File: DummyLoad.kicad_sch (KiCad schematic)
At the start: 31 parts, among them J1 RF In, J2 RF Out, J3 Conn_01x02_Pin

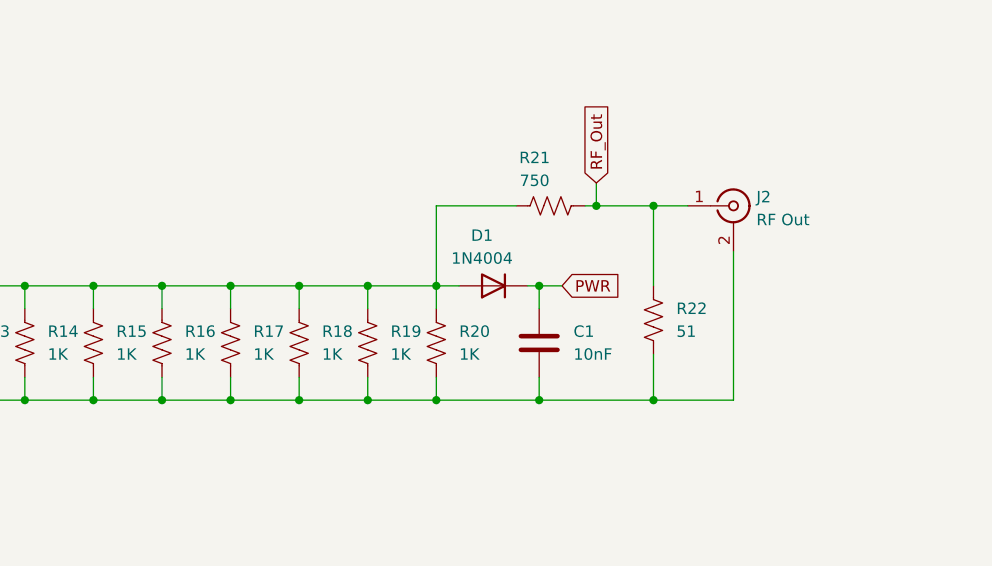
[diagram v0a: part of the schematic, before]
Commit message: Schematic: add symbols, ground & rewire
Modify DummyLoad.kicad_sch: add new symbols and power net, reposition several components and update wiring/junctions. Added Device:R_US instances (R24, R23), a power:GND symbol that creates a global GND label, and multiple junction/wire elements to re-route nets (including RF_Out and PWR). Removed a few redundant junctions/wires and updated component coordinates/UUIDs to reflect the new layout. These changes reorganize the sheet wiring and place new parts for the updated schematic topology.
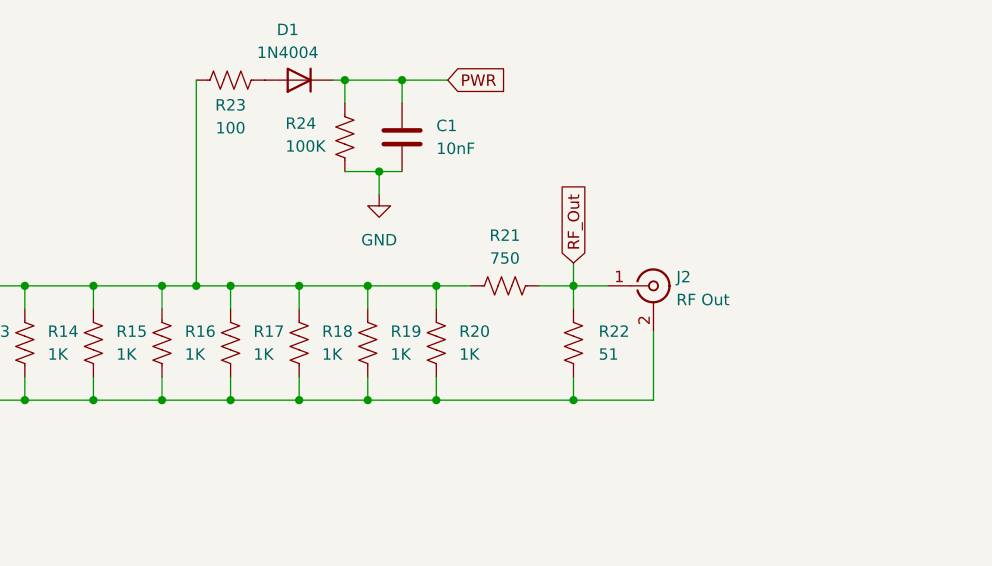
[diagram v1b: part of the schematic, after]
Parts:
- added R23: 100, symbol Device:R_US
- added R24: 100K, symbol Device:R_US
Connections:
- net GND: now also R24.2
- net PWR: now also R24.1
- net RF_In: now also R23.2; no longer D1.2 (A)
- new net: D1.2 (A), R23.1
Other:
- moved on the sheet: C1, D1, J2, R21, R22

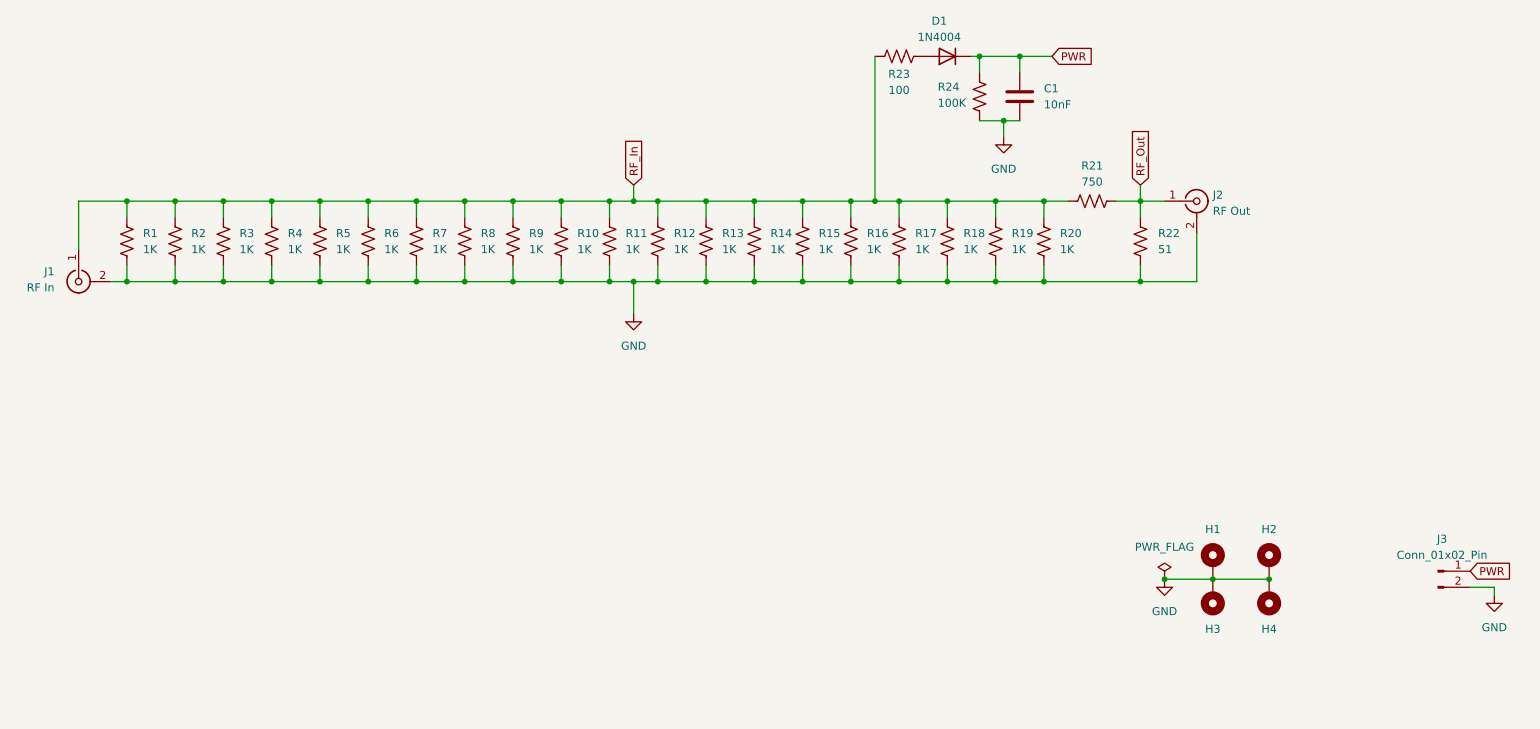
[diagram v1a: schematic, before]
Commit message: Schematic: update layout & title block
Set paper to USLetter and add a title block (title, date, revision, company and descriptive comments). Perform a large schematic redraw: many junctions, wires and their coordinates were moved and multiple UUIDs updated/renamed. Changes appear to be layout/coordinate and metadata updates rather than functional/electrical modifications.
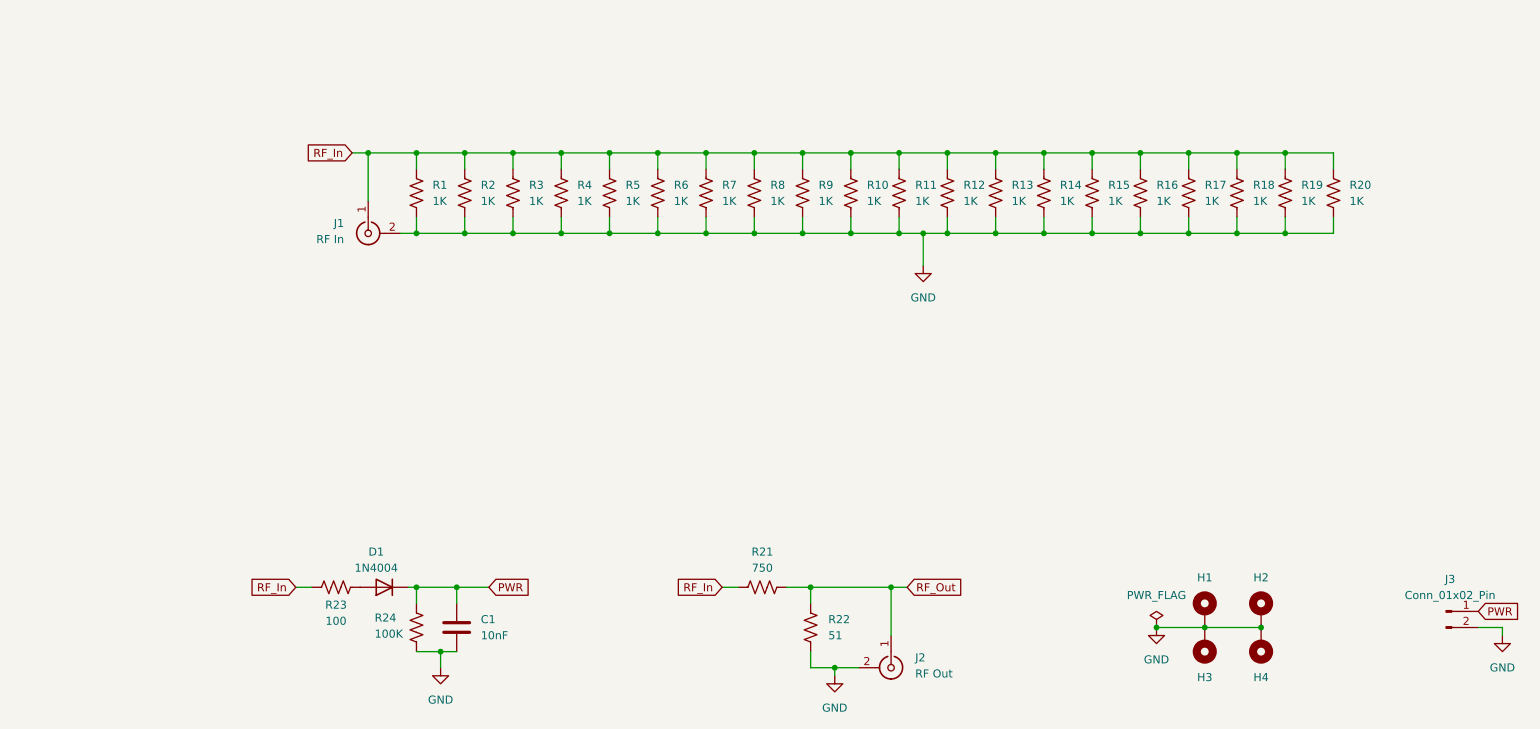
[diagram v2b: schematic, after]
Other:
- company: (none) -> NE3U
- title: (none) -> Dummy Load
- moved on the sheet: C1, D1, H1, H2, H3, H4, J1, J2, J3, R1, R10, R11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

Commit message: Refactor connector, testpoints and layout
Replace generic connector symbols with coaxial/TestPoint symbols and tidy schematic metadata; adjust component positions, wires and junctions, and update footprints/datasheets/Mouser PNs. Added text annotations (Mounting Holes, 50 Ohm Dummy Load, attenuation/measurement notes), new testpoint symbols/instances and a few resistor symbols/instances, renamed/updated some references (e.g. R24 -> R26) and moved mounting holes and global label locations to match the revised layout. These changes improve part accuracy, footprints and documentation in the DummyLoad.kicad_sch.
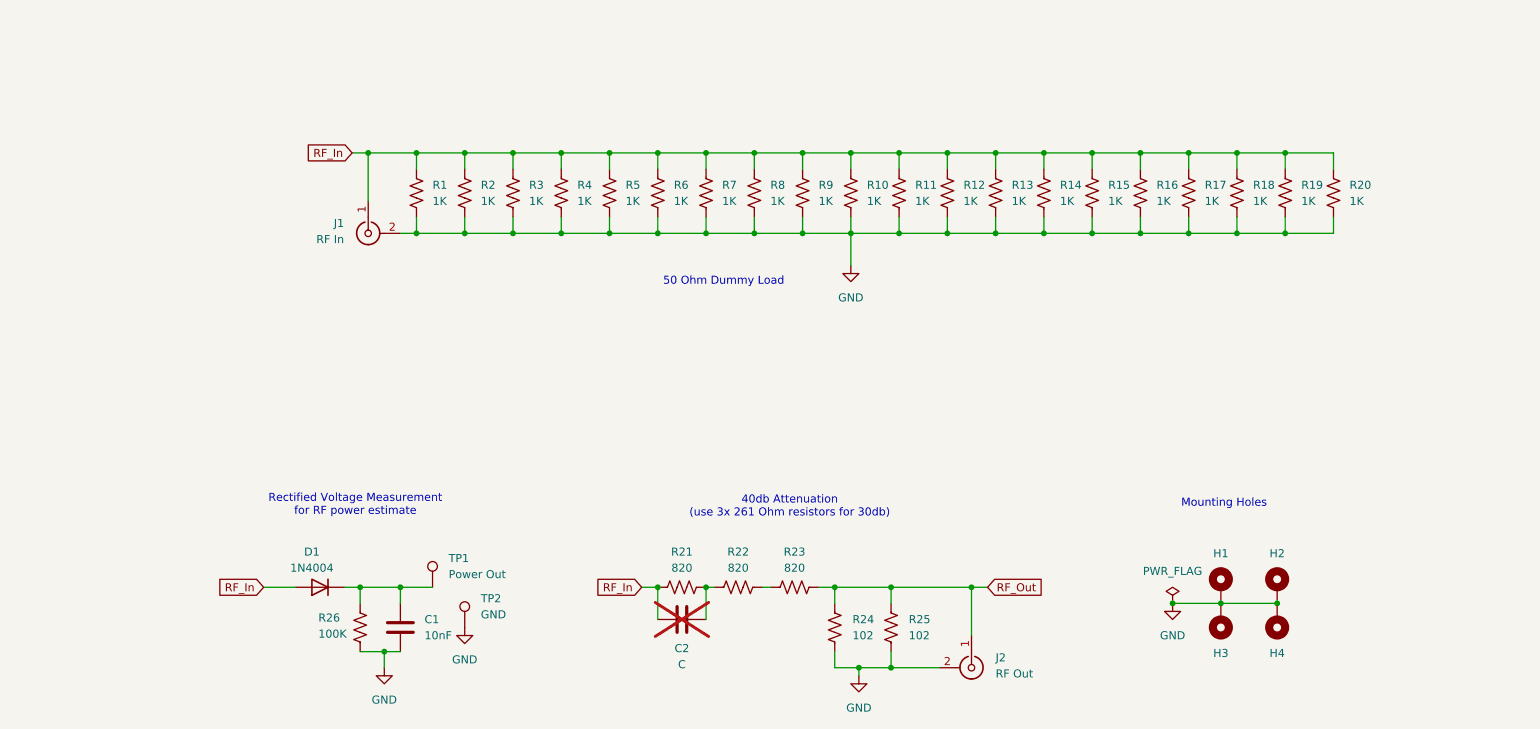
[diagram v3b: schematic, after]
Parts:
- removed J3: Conn_01x02_Pin, Connector_PinHeader_2.54mm:PinHeader_1x02_P2.54mm_Vertical, symbol Connector:Conn_01x02_Pin
- removed R23: 100, symbol Device:R_US
- added C2: C, Capacitor_SMD:C_1206_3216Metric, symbol Device:C
- added R21, R22: 820, Resistor_SMD:R_1206_3216Metric, symbol Device:R_US
- added R25: 102, Resistor_SMD:R_1206_3216Metric, symbol Device:R_US
- added TP1: Power Out, symbol Connector:TestPoint
- added TP2: GND, symbol Connector:TestPoint
- C1: Mouser PN (none) -> 77-VJ1206Y103JXAMP
- D1: Mouser PN (none) -> 583-FM4004
- J1, J2: Mouser PN (none) -> 737-RF101KD0050BKHDW
- R23: renamed from R21; value 750 -> 820; Mouser PN 708-RNCP1206FTD750R -> 279-CRGH1206F820R
- R24: renamed from R22; value 51 -> 102; Mouser PN (none) -> 667-ERJ-8ENF1020V
- R26: renamed from R24; footprint (none) -> Resistor_SMD:R_1206_3216Metric; Mouser PN (none) -> 652-CRM1206QFX-1003E
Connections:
- net GND: now also R25.2, TP2.1
- net RF_In: now also D1.2 (A), C2.2, R21.2; no longer R23.2
- net RF_Out: now also R25.1
- net PWR: no longer names the net of C1.1, D1.1 (K), R26.1
- net PWR: now also TP1.1
- new net: R22.1, R23.2
- new net: C2.1, R21.1, R22.2
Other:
- note added: "40db Attenuation (use 3x 261 Ohm resistors for 30db)"
- note added: "50 Ohm Dummy Load"
- note added: "Mounting Holes"
- note added: "Rectified Voltage Measurement for RF power estimate"
- company: NE3U -> Design by NE3U
- moved on the sheet: C1, D1, H1, H2, H3, H4, J2, R23, R24, R26

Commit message: Add THT test point footprints to schematic
Assign the TestPoint footprint to two components in DummyLoad.kicad_sch. Previously the Footprint property was empty; this commit sets it to "TestPoint:TestPoint_THTPad_D1.0mm_Drill0.5mm" for the two entries so exported netlists/PCBs include the intended through-hole test pads.
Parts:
- TP1, TP2: footprint (none) -> TestPoint:TestPoint_THTPad_D1.0mm_Drill0.5mm
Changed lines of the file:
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@@
 			)
 		)
-		(property "Footprint" ""
+		(property "Footprint" "TestPoint:TestPoint_THTPad_D1.0mm_Drill0.5mm"
 			(at 91.44 127 0)
 			(effects
@@
 			)
 		)
-		(property "Footprint" ""
+		(property "Footprint" "TestPoint:TestPoint_THTPad_D1.0mm_Drill0.5mm"
 			(at 86.36 120.65 0)
 			(effects

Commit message: Update component datasheets, PNs, footprints
Update metadata in DummyLoad.kicad_sch: replace generic Vishay datasheet links with the direct rcse3.pdf URL and change Mouser PN from 279-CRGP2512F1K0 to 71-RCS12061K00FKEA across multiple components. Also update one diode entry: change footprint to Diode_SMD:Nexperia_CFP3_SOD-123W, datasheet to 1N5711W.pdf, and Mouser PN to 621-1N5711W-F. These changes correct BOM/reference links and footprints for accurate sourcing.
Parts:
- D1: footprint Diode_SMD:D_SMA -> Diode_SMD:Nexperia_CFP3_SOD-123W; Mouser PN 583-FM4004 -> 621-1N5711W-F
- R1, R10, R11, R12, R13, R14, R15, R16, R17, R18, R19, R2, R20, R3, R4, R5, R6, R7, R8, R9: Mouser PN 279-CRGP2512F1K0 -> 71-RCS12061K00FKEA
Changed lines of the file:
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@@
 			)
 		)
-		(property "Datasheet" "https://www.vishay.com/doc?20065"
+		(property "Datasheet" "https://www.vishay.com/docs/20065/rcse3.pdf"
 			(at 147.32 58.42 0)
 			(effects
@@
 			)
 		)
-		(property "Mouser PN" "279-CRGP2512F1K0"
+		(property "Mouser PN" "71-RCS12061K00FKEA"
 			(at 147.32 58.42 0)
 			(effects
@@
 			)
 		)
-		(property "Datasheet" "https://www.vishay.com/doc?20065"
+		(property "Datasheet" "https://www.vishay.com/docs/20065/rcse3.pdf"
 			(at 162.56 58.42 0)
 			(effects
@@
 			)
 		)
-		(property "Mouser PN" "279-CRGP2512F1K0"
+		(property "Mouser PN" "71-RCS12061K00FKEA"
 			(at 162.56 58.42 0)
 			(effects
@@
 			)
 		)
-		(property "Datasheet" "https://www.vishay.com/doc?20065"
+		(property "Datasheet" "https://www.vishay.com/docs/20065/rcse3.pdf"
 			(at 139.7 58.42 0)
 			(effects
@@
 			)
 		)
-		(property "Mouser PN" "279-CRGP2512F1K0"
+		(property "Mouser PN" "71-RCS12061K00FKEA"
 			(at 139.7 58.42 0)
 			(effects
@@
 			)
 		)
-		(property "Datasheet" "https://www.vishay.com/doc?20065"
+		(property "Datasheet" "https://www.vishay.com/docs/20065/rcse3.pdf"
 			(at 78.74 58.42 0)
 			(effects
@@
 			)
 		)
-		(property "Mouser PN" "279-CRGP2512F1K0"
+		(property "Mouser PN" "71-RCS12061K00FKEA"
 			(at 78.74 58.42 0)
 			(effects
@@
 			)
 		)
-		(property "Datasheet" "https://www.vishay.com/doc?20065"
+		(property "Datasheet" "https://www.vishay.com/docs/20065/rcse3.pdf"
 			(at 86.36 58.42 0)
 			(effects
@@
 			)
 		)
-		(property "Mouser PN" "279-CRGP2512F1K0"
+		(property "Mouser PN" "71-RCS12061K00FKEA"
 			(at 86.36 58.42 0)
 			(effects
@@
 			)
 		)
-		(property "Datasheet" "https://www.vishay.com/doc?20065"
+		(property "Datasheet" "https://www.vishay.com/docs/20065/rcse3.pdf"
 			(at 109.22 58.42 0)
 			(effects
@@
 			)
 		)
-		(property "Mouser PN" "279-CRGP2512F1K0"
+		(property "Mouser PN" "71-RCS12061K00FKEA"
 			(at 109.22 58.42 0)
 			(effects
@@
 			)
 		)
-		(property "Datasheet" "https://www.vishay.com/doc?20065"
+		(property "Datasheet" "https://www.vishay.com/docs/20065/rcse3.pdf"
 			(at 215.9 58.42 0)
 			(effects
@@
 			)
 		)
-		(property "Mouser PN" "279-CRGP2512F1K0"
+		(property "Mouser PN" "71-RCS12061K00FKEA"
 			(at 215.9 58.42 0)
 			(effects
@@
 			)
 		)
-		(property "Datasheet" "https://www.vishay.com/doc?20065"
+		(property "Datasheet" "https://www.vishay.com/docs/20065/rcse3.pdf"
 			(at 177.8 58.42 0)
 			(effects
@@
 			)
 		)
-		(property "Mouser PN" "279-CRGP2512F1K0"
+		(property "Mouser PN" "71-RCS12061K00FKEA"
 			(at 177.8 58.42 0)
 			(effects
@@
 			)
 		)
-		(property "Datasheet" "https://www.vishay.com/doc?20065"
+		(property "Datasheet" "https://www.vishay.com/docs/20065/rcse3.pdf"
 			(at 93.98 58.42 0)
 			(effects
@@
 			)
 		)
-		(property "Mouser PN" "279-CRGP2512F1K0"
+		(property "Mouser PN" "71-RCS12061K00FKEA"
 			(at 93.98 58.42 0)
 			(effects
@@
 			)
 		)
-		(property "Datasheet" "https://www.vishay.com/doc?20065"
+		(property "Datasheet" "https://www.vishay.com/docs/20065/rcse3.pdf"
 			(at 170.18 58.42 0)
 			(effects
@@
 			)
 		)
-		(property "Mouser PN" "279-CRGP2512F1K0"
+		(property "Mouser PN" "71-RCS12061K00FKEA"
 			(at 170.18 58.42 0)
 			(effects
@@
 			)
 		)
-		(property "Datasheet" "https://www.vishay.com/doc?20065"
+		(property "Datasheet" "https://www.vishay.com/docs/20065/rcse3.pdf"
 			(at 116.84 58.42 0)
 			(effects
@@
 			)
 		)
-		(property "Mouser PN" "279-CRGP2512F1K0"
+		(property "Mouser PN" "71-RCS12061K00FKEA"
 			(at 116.84 58.42 0)
 			(effects
@@
 			)
 		)
-		(property "Datasheet" "https://www.vishay.com/doc?20065"
+		(property "Datasheet" "https://www.vishay.com/docs/20065/rcse3.pdf"
 			(at 208.28 58.42 0)
 			(effects
@@
 			)
 		)
-		(property "Mouser PN" "279-CRGP2512F1K0"
+		(property "Mouser PN" "71-RCS12061K00FKEA"
 			(at 208.28 58.42 0)
 			(effects
@@
 			)
 		)
-		(property "Datasheet" "https://www.vishay.com/doc?20065"
+		(property "Datasheet" "https://www.vishay.com/docs/20065/rcse3.pdf"
 			(at 101.6 58.42 0)
 			(effects
@@
 			)
 		)
-		(property "Mouser PN" "279-CRGP2512F1K0"
+		(property "Mouser PN" "71-RCS12061K00FKEA"
 			(at 101.6 58.42 0)
 			(effects
@@
 			)
 		)
-		(property "Datasheet" "https://www.vishay.com/doc?20065"
+		(property "Datasheet" "https://www.vishay.com/docs/20065/rcse3.pdf"
 			(at 185.42 58.42 0)
 			(effects
@@
 			)
 		)
-		(property "Mouser PN" "279-CRGP2512F1K0"
+		(property "Mouser PN" "71-RCS12061K00FKEA"
 			(at 185.42 58.42 0)
 			(effects
@@
 			)
 		)
-		(property "Datasheet" "https://www.vishay.com/doc?20065"
+		(property "Datasheet" "https://www.vishay.com/docs/20065/rcse3.pdf"
 			(at 124.46 58.42 0)
 			(effects
@@
 			)
 		)
-		(property "Mouser PN" "279-CRGP2512F1K0"
+		(property "Mouser PN" "71-RCS12061K00FKEA"
 			(at 124.46 58.42 0)
 			(effects
@@
 			)
 		)
-		(property "Datasheet" "https://www.vishay.com/doc?20065"
+		(property "Datasheet" "https://www.vishay.com/docs/20065/rcse3.pdf"
 			(at 132.08 58.42 0)
 			(effects
@@
 			)
 		)
-		(property "Mouser PN" "279-CRGP2512F1K0"
+		(property "Mouser PN" "71-RCS12061K00FKEA"
 			(at 132.08 58.42 0)
 			(effects
@@
 			)
 		)
-		(property "Datasheet" "https://www.vishay.com/doc?20065"
+		(property "Datasheet" "https://www.vishay.com/docs/20065/rcse3.pdf"
 			(at 200.66 58.42 0)
 			(effects
@@
 			)
 		)
-		(property "Mouser PN" "279-CRGP2512F1K0"
+		(property "Mouser PN" "71-RCS12061K00FKEA"
 			(at 200.66 58.42 0)
 			(effects
@@
 			)
 		)
-		(property "Datasheet" "https://www.vishay.com/doc?20065"
+		(property "Datasheet" "https://www.vishay.com/docs/20065/rcse3.pdf"
 			(at 154.94 58.42 0)
 			(effects
@@
 			)
 		)
-		(property "Mouser PN" "279-CRGP2512F1K0"
+		(property "Mouser PN" "71-RCS12061K00FKEA"
 			(at 154.94 58.42 0)
 			(effects
@@
 			)
 		)
-		(property "Footprint" "Diode_SMD:D_SMA"
+		(property "Footprint" "Diode_SMD:Nexperia_CFP3_SOD-123W"
 			(at 63.5 120.65 0)
 			(effects
@@
 			)
 		)
-		(property "Datasheet" "https://www.mouser.com/datasheet/3/287/1/fm4001_fm4007.pdf"
+		(property "Datasheet" "https://www.mouser.com/datasheet/3/175/1/1N5711W.pdf"
 			(at 63.5 120.65 0)
 			(effects
@@
 			)
 		)
-		(property "Mouser PN" "583-FM4004"
+		(property "Mouser PN" "621-1N5711W-F"
 			(at 63.5 120.65 0)
 			(effects
@@
 			)
 		)
-		(property "Datasheet" "https://www.vishay.com/doc?20065"
+		(property "Datasheet" "https://www.vishay.com/docs/20065/rcse3.pdf"
 			(at 223.52 58.42 0)
 			(effects
@@
 			)
 		)
-		(property "Mouser PN" "279-CRGP2512F1K0"
+		(property "Mouser PN" "71-RCS12061K00FKEA"
 			(at 223.52 58.42 0)
 			(effects
@@
 			)
 		)
-		(property "Datasheet" "https://www.vishay.com/doc?20065"
+		(property "Datasheet" "https://www.vishay.com/docs/20065/rcse3.pdf"
 			(at 193.04 58.42 0)
 			(effects
@@
 			)
 		)
-		(property "Mouser PN" "279-CRGP2512F1K0"
+		(property "Mouser PN" "71-RCS12061K00FKEA"
 			(at 193.04 58.42 0)
 			(effects

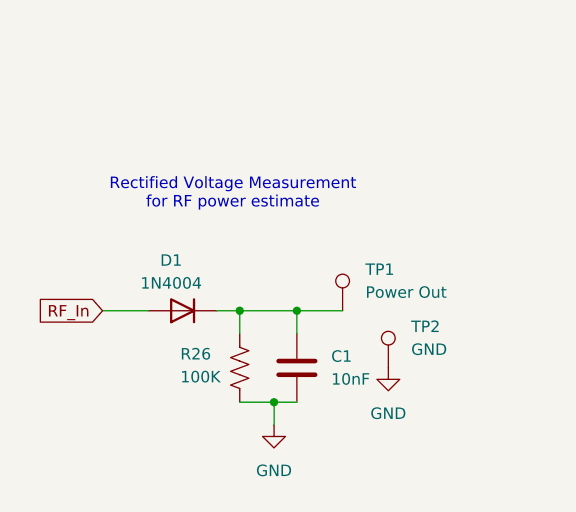
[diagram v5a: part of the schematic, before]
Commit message: Change diode value to 1N5711
Update the diode 'Value' property from 1N4004 to 1N5711 in both the KiCad schematic and PCB files (DummyLoad.kicad_sch and DummyLoad.kicad_pcb) so the schematic and board reflect the new component selection.
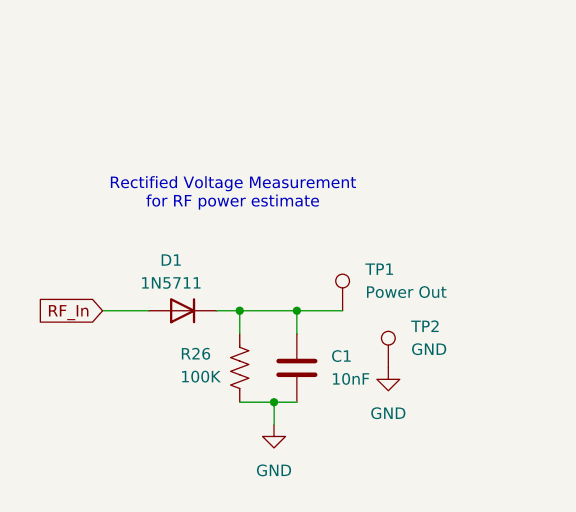
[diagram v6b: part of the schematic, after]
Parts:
- D1: value 1N4004 -> 1N5711
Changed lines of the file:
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@@
 			)
 		)
-		(property "Value" "1N4004"
+		(property "Value" "1N5711"
 			(at 62.23 117.602 0)
 			(effects
